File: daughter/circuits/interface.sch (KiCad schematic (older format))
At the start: 25 parts, among them J17 Conn_01x08, J18 C1, J19 Conn_01x08, J20 Conn_01x20, J21 Conn_01x20, J22 Conn_IDE_40, J23 Conn_01x08, J24 C2, J25 Conn_01x08, J26 Conn_01x20, J27 Conn_IDE_40, J28 Conn_01x20, J29 Conn_01x08, J30 C3, J31 Conn_01x08, J32 Conn_IDE_40, J33 Conn_01x20, J34 Conn_01x20, J35 Conn_01x12, J36 STEREO, J37 Conn_01x12, J38 Conn_01x01_Female, J39 Conn_01x01_Female, J40 Conn_01x01_Female, J41 Conn_01x01_Female

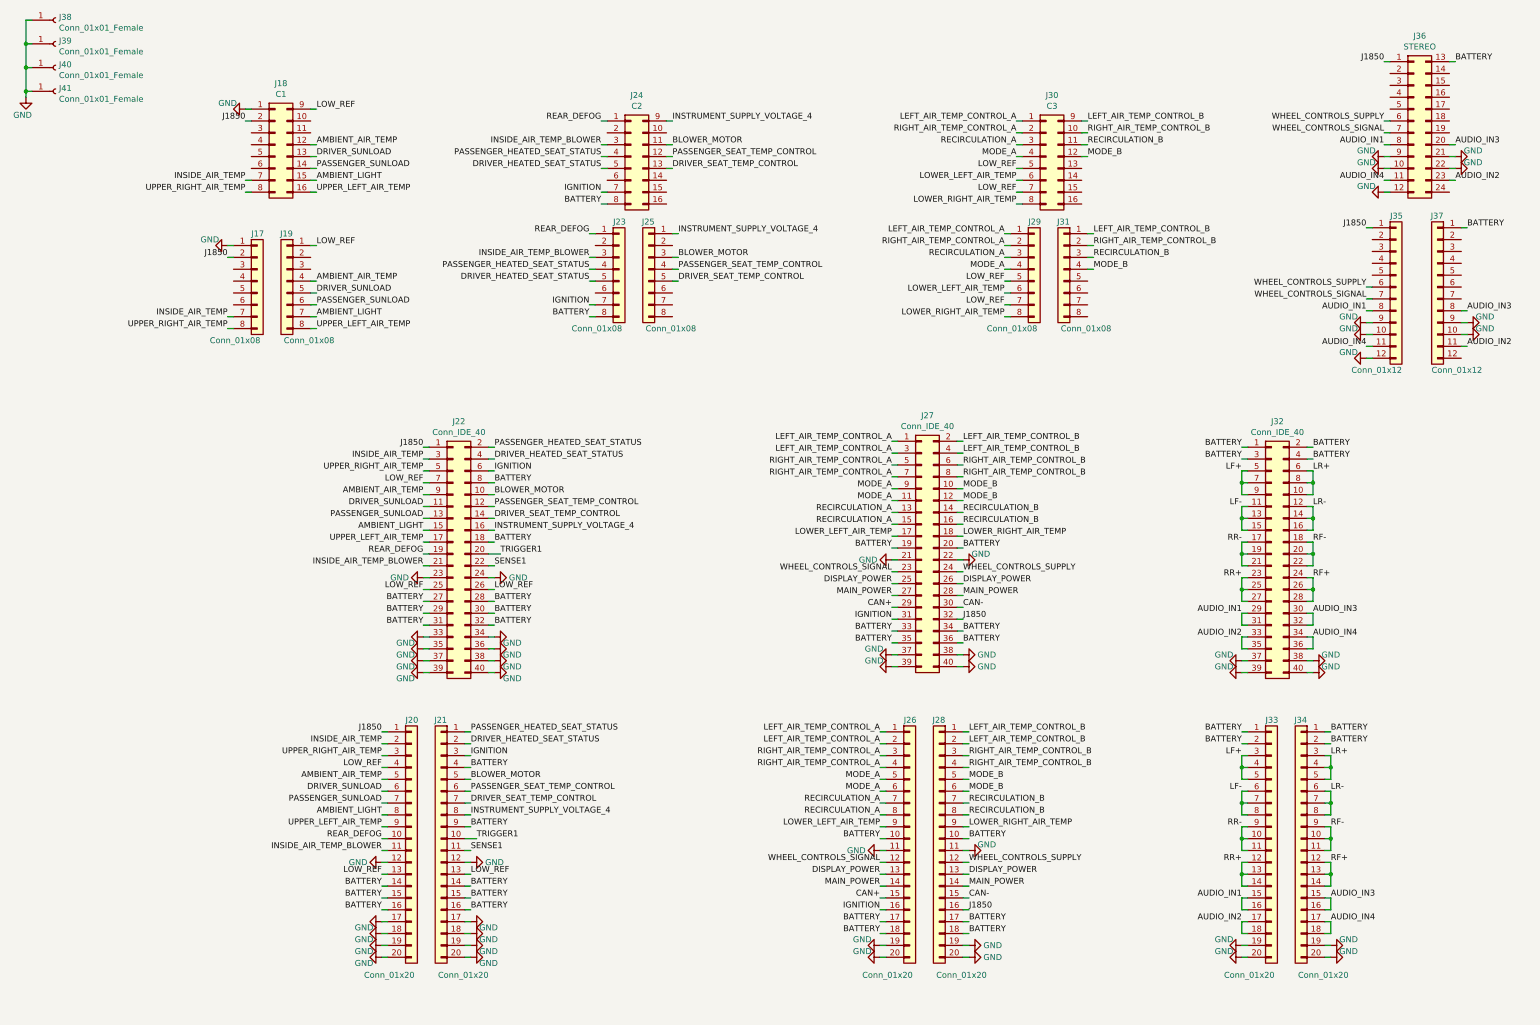
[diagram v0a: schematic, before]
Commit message: finished schematic, working on layout
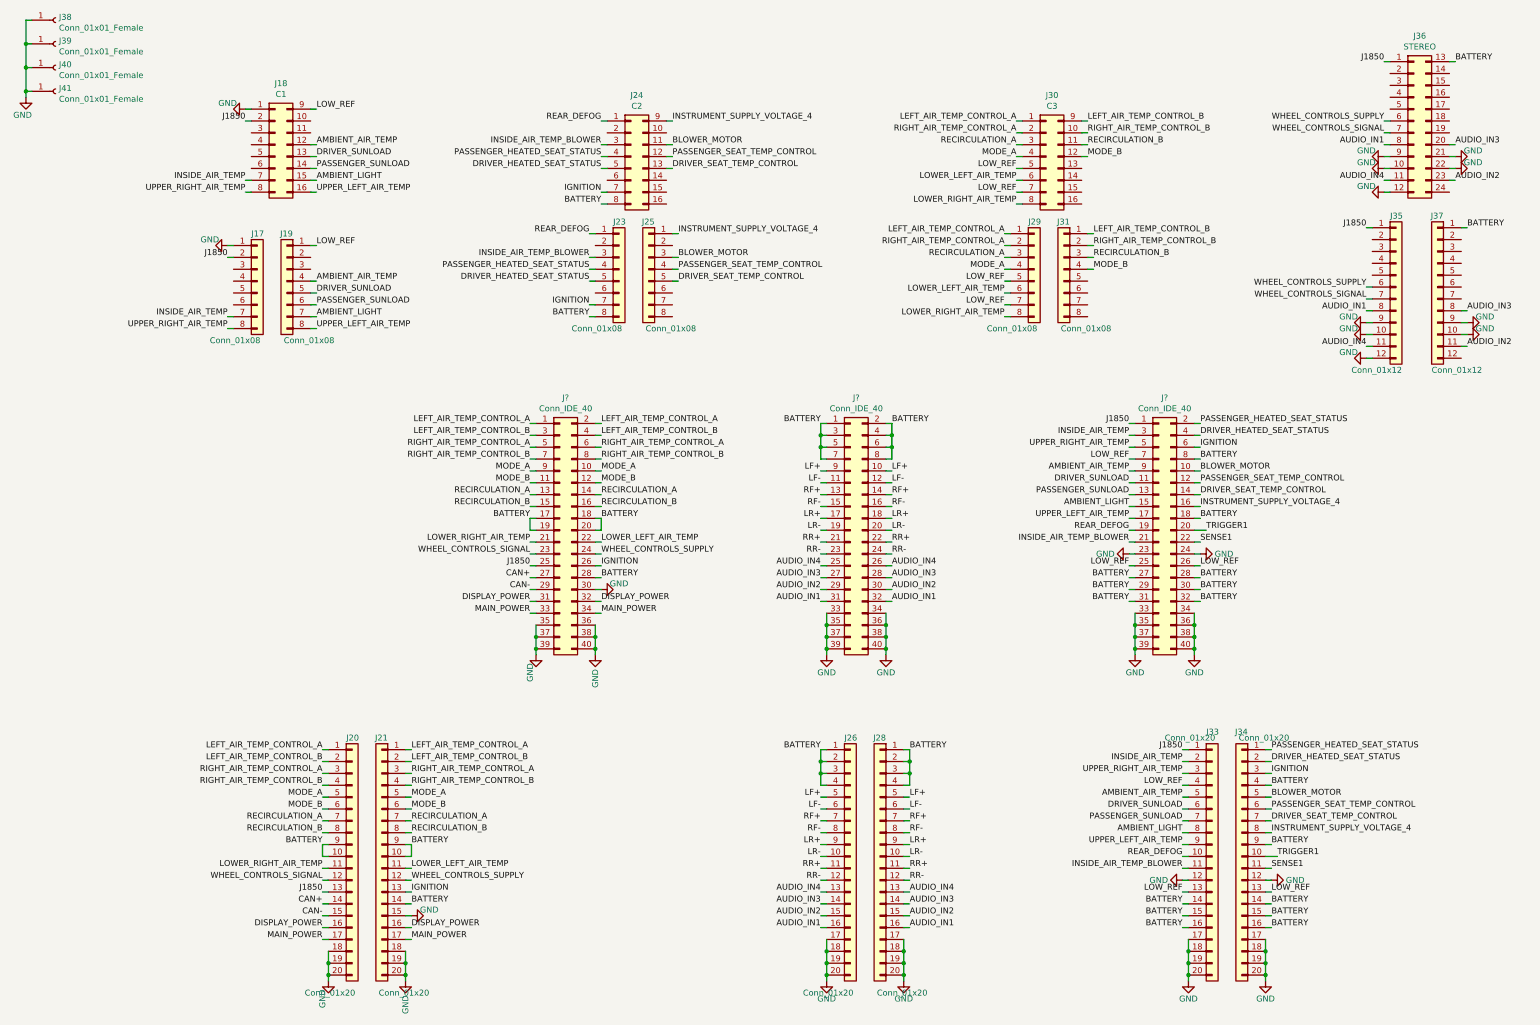
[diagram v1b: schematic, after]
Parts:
- removed J22, J27, J32: Conn_IDE_40, Connector_IDC:IDC-Header_2x20_P2.54mm_Vertical, symbol Open_Automation:Conn_IDE_40
- added J? (x3): Conn_IDE_40, Connector_IDC:IDC-Header_2x20_P2.54mm_Vertical, symbol Open_Automation:Conn_IDE_40
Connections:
- net AMBIENT_AIR_TEMP: now also J33.5 (Pin_5), J?.9 (Pin_9); no longer J20.5 (Pin_5)
- net AMBIENT_LIGHT: now also J33.8 (Pin_8), J?.15 (Pin_15); no longer J20.8 (Pin_8)
- net AUDIO_IN1: now also J26.16 (Pin_16), J28.16 (Pin_16), J?.31 (Pin_31), J?.32 (Pin_32); no longer J33.15 (Pin_15), J33.16 (Pin_16)
- net AUDIO_IN2: now also J26.15 (Pin_15), J28.15 (Pin_15), J?.29 (Pin_29), J?.30 (Pin_30); no longer J33.17 (Pin_17), J33.18 (Pin_18)
- net AUDIO_IN3: now also J26.14 (Pin_14), J28.14 (Pin_14), J?.27 (Pin_27), J?.28 (Pin_28); no longer J34.15 (Pin_15), J34.16 (Pin_16)
- net AUDIO_IN4: now also J26.13 (Pin_13), J28.13 (Pin_13), J?.25 (Pin_25), J?.26 (Pin_26); no longer J34.17 (Pin_17), J34.18 (Pin_18)
- net BATTERY: now also J20.10 (Pin_10), J20.9 (Pin_9), J21.10 (Pin_10), J26.1 (Pin_1), J26.2 (Pin_2), J26.3 (Pin_3), J26.4 (Pin_4), J28.1 (Pin_1), J28.2 (Pin_2), J28.3 (Pin_3), J28.4 (Pin_4), J33.14 (Pin_14), J33.15 (Pin_15), J33.16 (Pin_16), J34.14 (Pin_14), J34.15 (Pin_15), J34.16 (Pin_16), J34.4 (Pin_4), J34.9 (Pin_9), J?.1 (Pin_1), J?.17 (Pin_17), J?.18 (Pin_18), J?.18 (Pin_18), J?.19 (Pin_19), J?.2 (Pin_2), J?.20 (Pin_20), J?.27 (Pin_27), J?.28 (Pin_28), J?.28 (Pin_28), J?.29 (Pin_29), J?.3 (Pin_3), J?.30 (Pin_30), J?.31 (Pin_31), J?.32 (Pin_32), J?.4 (Pin_4), J?.5 (Pin_5), J?.6 (Pin_6), J?.7 (Pin_7), J?.8 (Pin_8), J?.8 (Pin_8); no longer J20.14 (Pin_14), J20.15 (Pin_15), J20.16 (Pin_16), J21.15 (Pin_15), J21.16 (Pin_16), J21.4 (Pin_4), J26.10 (Pin_10), J26.17 (Pin_17), J26.18 (Pin_18), J28.10 (Pin_10), J28.17 (Pin_17), J28.18 (Pin_18), J33.1 (Pin_1), J33.2 (Pin_2), J34.1 (Pin_1), J34.2 (Pin_2)
- net BLOWER_MOTOR: now also J34.5 (Pin_5), J?.10 (Pin_10); no longer J21.5 (Pin_5)
- net CAN+: now also J20.14 (Pin_14), J?.27 (Pin_27); no longer J26.15 (Pin_15)
- net CAN-: now also J20.15 (Pin_15), J?.29 (Pin_29); no longer J28.15 (Pin_15)
- net DISPLAY_POWER: now also J20.16 (Pin_16), J21.16 (Pin_16), J?.31 (Pin_31), J?.32 (Pin_32); no longer J26.13 (Pin_13), J28.13 (Pin_13)
- net DRIVER_HEATED_SEAT_STATUS: now also J34.2 (Pin_2), J?.4 (Pin_4); no longer J21.2 (Pin_2)
- net DRIVER_SEAT_TEMP_CONTROL: now also J34.7 (Pin_7), J?.14 (Pin_14); no longer J21.7 (Pin_7)
- net DRIVER_SUNLOAD: now also J33.6 (Pin_6), J?.11 (Pin_11); no longer J20.6 (Pin_6)
- net GND: now also J21.15 (Pin_15), J26.17 (Pin_17), J26.18 (Pin_18), J28.17 (Pin_17), J28.18 (Pin_18), J33.12 (Pin_12), J33.17 (Pin_17), J33.18 (Pin_18), J34.12 (Pin_12), J34.17 (Pin_17), J34.18 (Pin_18), J?.23 (Pin_23), J?.24 (Pin_24), J?.30 (Pin_30), J?.33 (Pin_33), J?.33 (Pin_33), J?.34 (Pin_34), J?.34 (Pin_34), J?.35 (Pin_35), J?.35 (Pin_35), J?.35 (Pin_35), J?.36 (Pin_36), J?.36 (Pin_36), J?.36 (Pin_36), J?.37 (Pin_37), J?.37 (Pin_37), J?.37 (Pin_37), J?.38 (Pin_38), J?.38 (Pin_38), J?.38 (Pin_38), J?.39 (Pin_39), J?.39 (Pin_39), J?.39 (Pin_39), J?.40 (Pin_40), J?.40 (Pin_40), J?.40 (Pin_40); no longer J20.12 (Pin_12), J20.17 (Pin_17), J21.12 (Pin_12), J21.17 (Pin_17), J26.11 (Pin_11), J28.11 (Pin_11)
- net IGNITION: now also J21.13 (Pin_13), J34.3 (Pin_3), J?.26 (Pin_26), J?.6 (Pin_6); no longer J21.3 (Pin_3), J26.16 (Pin_16)
- net INSIDE_AIR_TEMP: now also J33.2 (Pin_2), J?.3 (Pin_3); no longer J20.2 (Pin_2)
- net INSIDE_AIR_TEMP_BLOWER: now also J33.11 (Pin_11), J?.21 (Pin_21); no longer J20.11 (Pin_11)
- net INSTRUMENT_SUPPLY_VOLTAGE_4: now also J34.8 (Pin_8), J?.16 (Pin_16); no longer J21.8 (Pin_8)
- net J1850: now also J20.13 (Pin_13), J33.1 (Pin_1), J?.1 (Pin_1), J?.25 (Pin_25); no longer J20.1 (Pin_1), J28.16 (Pin_16)
- net LEFT_AIR_TEMP_CONTROL_A: now also J20.1 (Pin_1), J21.1 (Pin_1), J?.1 (Pin_1), J?.2 (Pin_2); no longer J26.1 (Pin_1), J26.2 (Pin_2)
- net LEFT_AIR_TEMP_CONTROL_B: now also J20.2 (Pin_2), J21.2 (Pin_2), J?.3 (Pin_3), J?.4 (Pin_4); no longer J28.1 (Pin_1), J28.2 (Pin_2)
- net LF+: now also J26.5 (Pin_5), J28.5 (Pin_5), J?.10 (Pin_10), J?.9 (Pin_9); no longer J33.3 (Pin_3), J33.4 (Pin_4), J33.5 (Pin_5)
- net LF-: now also J26.6 (Pin_6), J28.6 (Pin_6), J?.11 (Pin_11), J?.12 (Pin_12); no longer J33.6 (Pin_6), J33.7 (Pin_7), J33.8 (Pin_8)
- net LOWER_LEFT_AIR_TEMP: now also J21.11 (Pin_11), J?.22 (Pin_22); no longer J26.9 (Pin_9)
- net LOWER_RIGHT_AIR_TEMP: now also J20.11 (Pin_11), J?.21 (Pin_21); no longer J28.9 (Pin_9)
- net LOW_REF: now also J33.13 (Pin_13), J33.4 (Pin_4), J34.13 (Pin_13), J?.25 (Pin_25), J?.26 (Pin_26), J?.7 (Pin_7); no longer J20.13 (Pin_13), J20.4 (Pin_4), J21.13 (Pin_13)
- net LR+: now also J26.9 (Pin_9), J28.9 (Pin_9), J?.17 (Pin_17), J?.18 (Pin_18); no longer J34.3 (Pin_3), J34.4 (Pin_4), J34.5 (Pin_5)
- net LR-: now also J26.10 (Pin_10), J28.10 (Pin_10), J?.19 (Pin_19), J?.20 (Pin_20); no longer J34.6 (Pin_6), J34.7 (Pin_7), J34.8 (Pin_8)
- net MAIN_POWER: now also J20.17 (Pin_17), J21.17 (Pin_17), J?.33 (Pin_33), J?.34 (Pin_34); no longer J26.14 (Pin_14), J28.14 (Pin_14)
- net MODE_A: now also J20.5 (Pin_5), J21.5 (Pin_5), J?.10 (Pin_10), J?.9 (Pin_9); no longer J26.5 (Pin_5), J26.6 (Pin_6)
- net MODE_B: now also J20.6 (Pin_6), J21.6 (Pin_6), J?.11 (Pin_11), J?.12 (Pin_12); no longer J28.5 (Pin_5), J28.6 (Pin_6)
- net PASSENGER_HEATED_SEAT_STATUS: now also J34.1 (Pin_1), J?.2 (Pin_2); no longer J21.1 (Pin_1)
- net PASSENGER_SEAT_TEMP_CONTROL: now also J34.6 (Pin_6), J?.12 (Pin_12); no longer J21.6 (Pin_6)
- net PASSENGER_SUNLOAD: now also J33.7 (Pin_7), J?.13 (Pin_13); no longer J20.7 (Pin_7)
- net REAR_DEFOG: now also J33.10 (Pin_10), J?.19 (Pin_19); no longer J20.10 (Pin_10)
- net RECIRCULATION_A: now also J20.7 (Pin_7), J21.7 (Pin_7), J?.13 (Pin_13), J?.14 (Pin_14); no longer J26.7 (Pin_7), J26.8 (Pin_8)
- net RECIRCULATION_B: now also J20.8 (Pin_8), J21.8 (Pin_8), J?.15 (Pin_15), J?.16 (Pin_16); no longer J28.7 (Pin_7), J28.8 (Pin_8)
- net RF+: now also J26.7 (Pin_7), J28.7 (Pin_7), J?.13 (Pin_13), J?.14 (Pin_14); no longer J34.12 (Pin_12), J34.13 (Pin_13), J34.14 (Pin_14)
- net RF-: now also J26.8 (Pin_8), J28.8 (Pin_8), J?.15 (Pin_15), J?.16 (Pin_16); no longer J34.10 (Pin_10), J34.11 (Pin_11), J34.9 (Pin_9)
- net RIGHT_AIR_TEMP_CONTROL_A: now also J20.3 (Pin_3), J21.3 (Pin_3), J?.5 (Pin_5), J?.6 (Pin_6); no longer J26.3 (Pin_3), J26.4 (Pin_4)
- net RIGHT_AIR_TEMP_CONTROL_B: now also J20.4 (Pin_4), J21.4 (Pin_4), J?.7 (Pin_7), J?.8 (Pin_8); no longer J28.3 (Pin_3), J28.4 (Pin_4)
- net RR+: now also J26.11 (Pin_11), J28.11 (Pin_11), J?.21 (Pin_21), J?.22 (Pin_22); no longer J33.12 (Pin_12), J33.13 (Pin_13), J33.14 (Pin_14)
- net RR-: now also J26.12 (Pin_12), J28.12 (Pin_12), J?.23 (Pin_23), J?.24 (Pin_24); no longer J33.10 (Pin_10), J33.11 (Pin_11), J33.9 (Pin_9)
- net SENSE1: now also J34.11 (Pin_11), J?.22 (Pin_22); no longer J21.11 (Pin_11)
- net TRIGGER1: now also J34.10 (Pin_10), J?.20 (Pin_20); no longer J21.10 (Pin_10)
- net UPPER_LEFT_AIR_TEMP: now also J33.9 (Pin_9), J?.17 (Pin_17); no longer J20.9 (Pin_9)
- net UPPER_RIGHT_AIR_TEMP: now also J33.3 (Pin_3), J?.5 (Pin_5); no longer J20.3 (Pin_3)
- net WHEEL_CONTROLS_SIGNAL: now also J20.12 (Pin_12), J?.23 (Pin_23); no longer J26.12 (Pin_12)
- net WHEEL_CONTROLS_SUPPLY: now also J21.12 (Pin_12), J?.24 (Pin_24); no longer J28.12 (Pin_12)
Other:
- moved on the sheet: J20, J21, J26, J28, J33, J34

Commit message: finished layout
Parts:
- gave numbers to parts that had none: 3
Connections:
- net LOW_REF is gone; now on net GND: J18.9 (Pin_9), J19.1 (Pin_1), J29.5 (Pin_5), J29.7 (Pin_7), J30.5 (Pin_5), J30.7 (Pin_7), J32.25 (Pin_25), J32.26 (Pin_26), J32.7 (Pin_7), J33.13 (Pin_13), J33.4 (Pin_4), J34.13 (Pin_13)
- net LF+: now also J26.9 (Pin_9), J27.17 (Pin_17), J27.18 (Pin_18), J28.9 (Pin_9); no longer J26.5 (Pin_5), J27.10 (Pin_10), J27.9 (Pin_9), J28.5 (Pin_5)
- net LF-: now also J26.10 (Pin_10), J27.19 (Pin_19), J27.20 (Pin_20), J28.10 (Pin_10); no longer J26.6 (Pin_6), J27.11 (Pin_11), J27.12 (Pin_12), J28.6 (Pin_6)
- net LR+: now also J26.8 (Pin_8), J27.15 (Pin_15), J27.16 (Pin_16), J28.8 (Pin_8); no longer J26.9 (Pin_9), J27.17 (Pin_17), J27.18 (Pin_18), J28.9 (Pin_9)
- net LR-: now also J26.7 (Pin_7), J27.13 (Pin_13), J27.14 (Pin_14), J28.7 (Pin_7); no longer J26.10 (Pin_10), J27.19 (Pin_19), J27.20 (Pin_20), J28.10 (Pin_10)
- net RF+: now also J26.11 (Pin_11), J27.21 (Pin_21), J27.22 (Pin_22), J28.11 (Pin_11); no longer J26.7 (Pin_7), J27.13 (Pin_13), J27.14 (Pin_14), J28.7 (Pin_7)
- net RF-: now also J26.12 (Pin_12), J27.23 (Pin_23), J27.24 (Pin_24), J28.12 (Pin_12); no longer J26.8 (Pin_8), J27.15 (Pin_15), J27.16 (Pin_16), J28.8 (Pin_8)
- net RR+: now also J26.6 (Pin_6), J27.11 (Pin_11), J27.12 (Pin_12), J28.6 (Pin_6); no longer J26.11 (Pin_11), J27.21 (Pin_21), J27.22 (Pin_22), J28.11 (Pin_11)
- net RR-: now also J26.5 (Pin_5), J27.10 (Pin_10), J27.9 (Pin_9), J28.5 (Pin_5); no longer J26.12 (Pin_12), J27.23 (Pin_23), J27.24 (Pin_24), J28.12 (Pin_12)

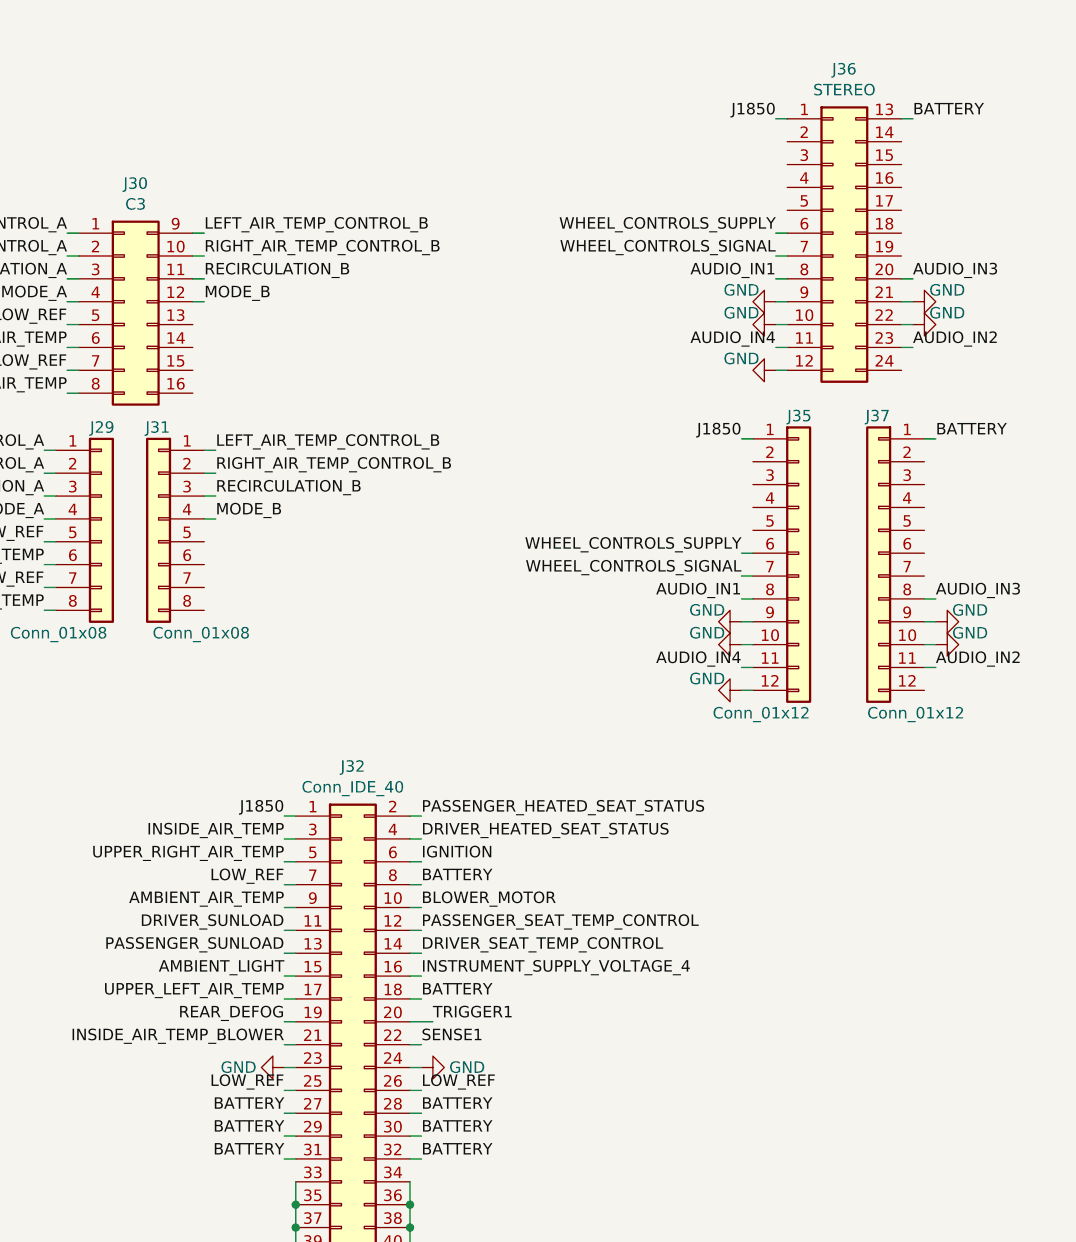
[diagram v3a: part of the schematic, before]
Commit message: Added external amp trigger code and circuit to PCB. Made some layout modifications.
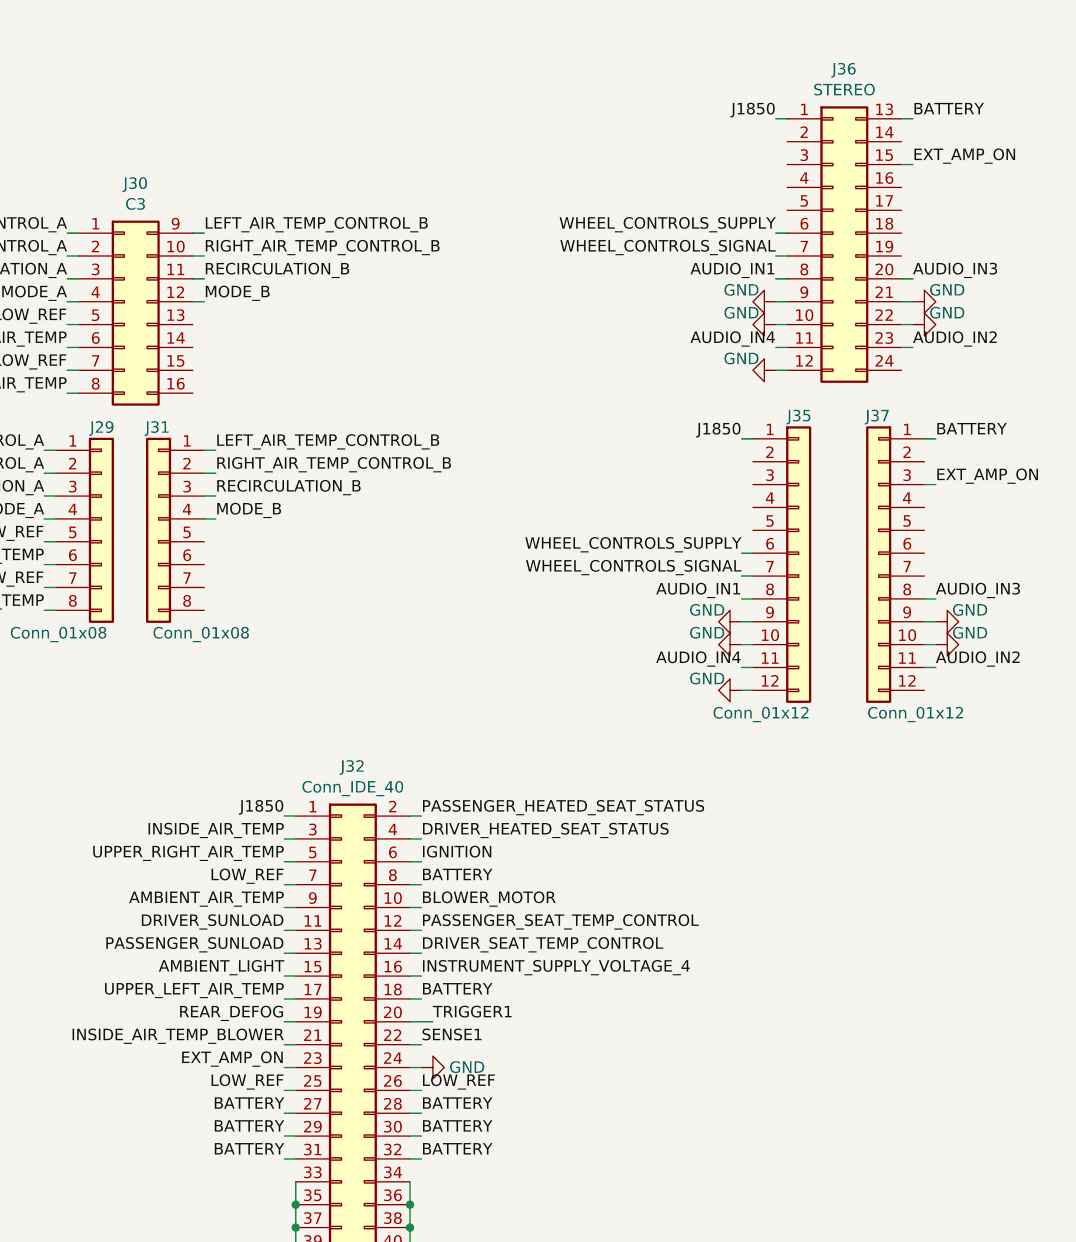
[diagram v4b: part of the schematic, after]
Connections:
- net GND: no longer J32.23 (Pin_23)
- net EXT_AMP_ON: now reaches J36.15 (Pin_15)
- net EXT_AMP_ON: now also J32.23 (Pin_23), J37.3 (Pin_3)
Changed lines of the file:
@@
 Wire Wire Line
 	11000 4200 10950 4200
-$Comp
-L open-dash-daughterboard-rescue:GND-power #PWR?
-U 1 1 6073066F
-P 10400 5300
-AR Path="/5ABD187E/6073066F" Ref="#PWR?"  Part="1"
-AR Path="/6073066F" Ref="#PWR?"  Part="1"
-AR Path="/5A7BADB8/6073066F" Ref="#PWR?"  Part="1"
-AR Path="/62CC146C/6073066F" Ref="#PWR?"  Part="1"
-AR Path="/657571BE/6073066F" Ref="#PWR0127"  Part="1"
-F 0 "#PWR0127" H 10400 5050 50  0001 C CNN
-F 1 "GND" V 10400 5100 50  0000 C CNN
-F 2 "" H 10400 5300 50  0001 C CNN
-F 3 "" H 10400 5300 50  0001 C CNN
-	1    10400 5300
-	0    1    1    0
-$EndComp
 Wire Wire Line
 	10400 5300 10450 5300
@@
 	0    -1   -1   0
 $EndComp
+Text Label 10400 5300 2    50   ~ 0
+EXT_AMP_ON
+Text Label 13250 2750 0    50   ~ 0
+EXT_AMP_ON
+Wire Wire Line
+	13250 2750 13200 2750
+Text Label 13150 1350 0    50   ~ 0
+EXT_AMP_ON
+Wire Wire Line
+	13150 1350 13100 1350
 $EndSCHEMATC
